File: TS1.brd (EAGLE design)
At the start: 32 x 22 mm, 20 parts, among them IC1 AT42QT1010, J1 PWR, Q1 2N7002

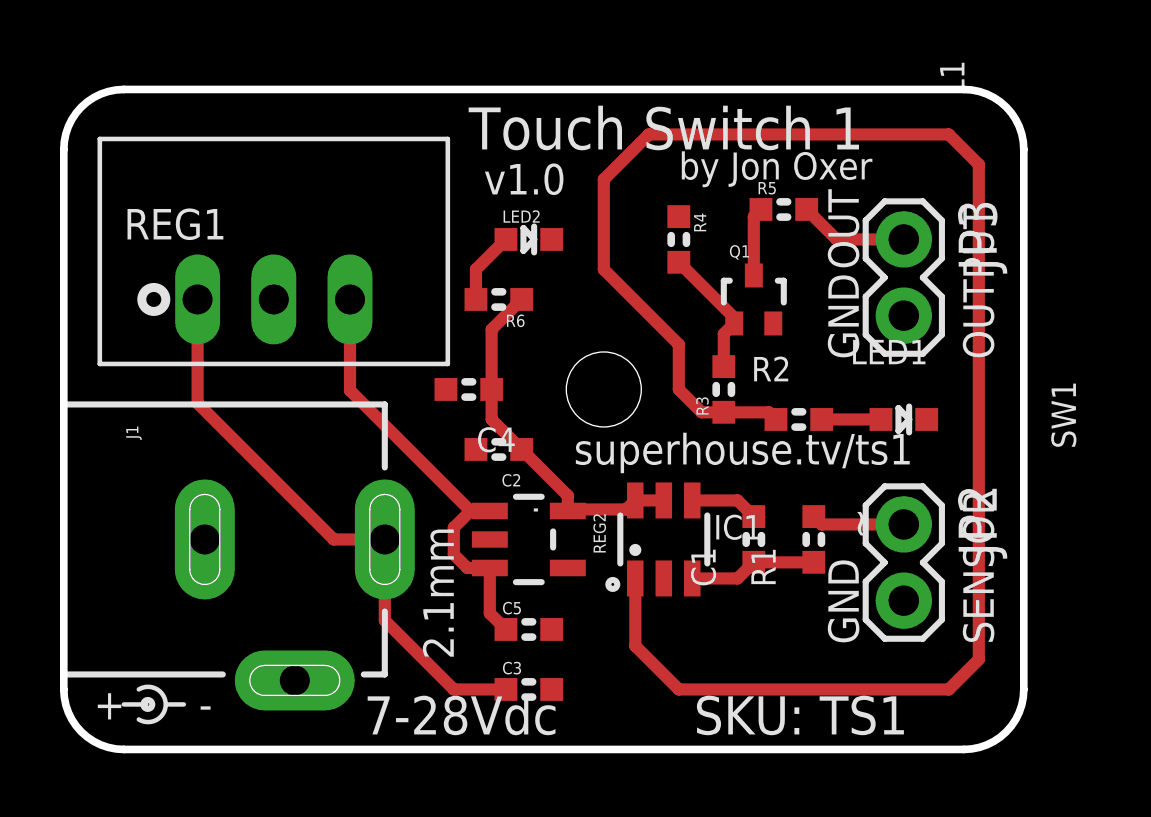
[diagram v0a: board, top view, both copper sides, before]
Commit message: Pulled back GND plane around input to sensor IC to reduce capacitive loading
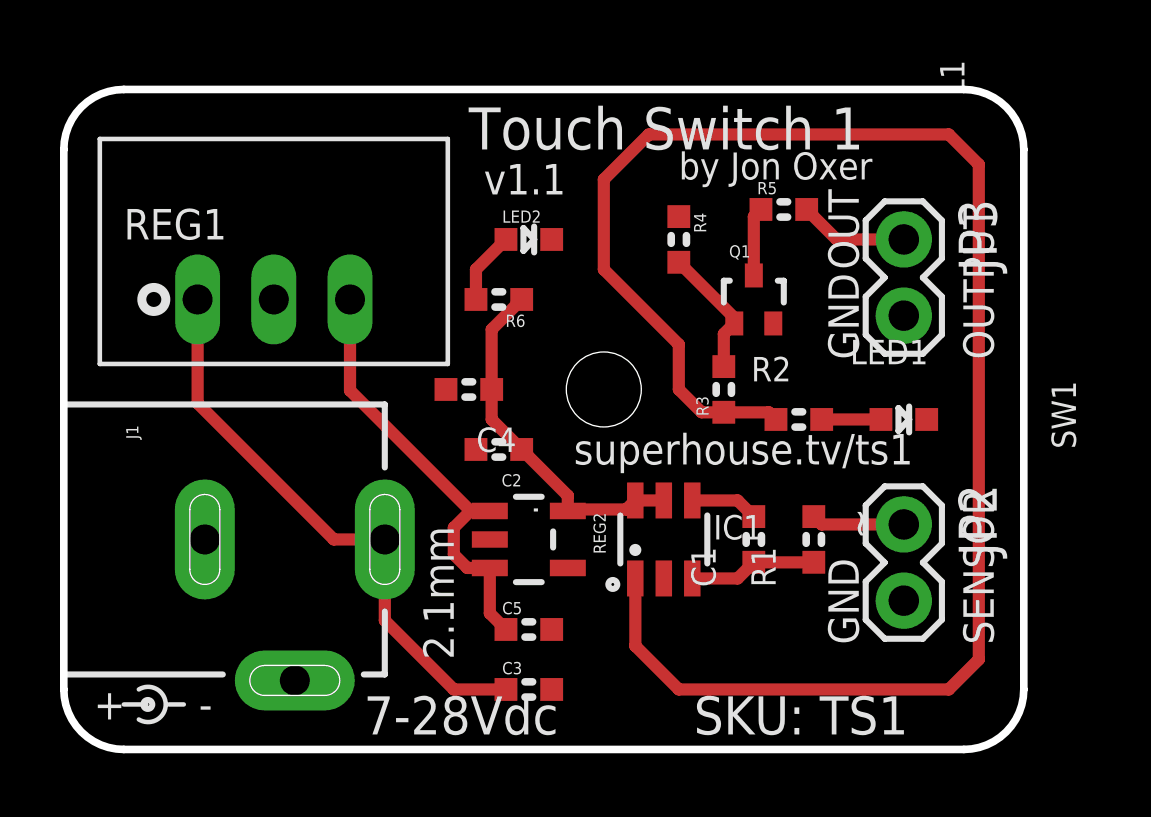
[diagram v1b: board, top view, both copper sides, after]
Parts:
- C2: value 10uF -> 100nF
- C4: value 100nF -> 10uF
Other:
- board text added: "Copyright 2019 SuperHouse Automation Pty Ltd"
- board text added: "v1.1"
- board text removed: "Copyright 2018 SuperHouse Automation Pty Ltd"
- board text removed: "v1.0"
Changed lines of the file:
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@@
 <?xml version="1.0" encoding="utf-8"?>
 <!DOCTYPE eagle SYSTEM "eagle.dtd">
-<eagle version="9.2.1">
+<eagle version="9.5.1">
 <drawing>
 <settings>
-<setting alwaysvectorfont="yes"/>
+<setting alwaysvectorfont="no"/>
 <setting keepoldvectorfont="yes"/>
 <setting verticaltext="up"/>
@@
 <layer number="14" name="Route14" color="1" fill="6" visible="no" active="no"/>
 <layer number="15" name="Route15" color="4" fill="6" visible="no" active="no"/>
-<layer number="16" name="Bottom" color="1" fill="1" visible="no" active="yes"/>
+<layer number="16" name="Bottom" color="1" fill="1" visible="yes" active="yes"/>
 <layer number="17" name="Pads" color="2" fill="1" visible="yes" active="yes"/>
 <layer number="18" name="Vias" color="2" fill="1" visible="yes" active="yes"/>
 <layer number="19" name="Unrouted" color="12" fill="1" visible="yes" active="yes"/>
 <layer number="20" name="Dimension" color="15" fill="1" visible="yes" active="yes"/>
-<layer number="21" name="tPlace" color="15" fill="1" visible="no" active="yes"/>
-<layer number="22" name="bPlace" color="14" fill="1" visible="no" active="yes"/>
+<layer number="21" name="tPlace" color="15" fill="1" visible="yes" active="yes"/>
+<layer number="22" name="bPlace" color="14" fill="1" visible="yes" active="yes"/>
 <layer number="23" name="tOrigins" color="15" fill="1" visible="yes" active="yes"/>
 <layer number="24" name="bOrigins" color="15" fill="1" visible="yes" active="yes"/>
@@
 <layer number="37" name="tTest" color="7" fill="1" visible="no" active="yes"/>
 <layer number="38" name="bTest" color="7" fill="1" visible="no" active="yes"/>
-<layer number="39" name="tKeepout" color="4" fill="11" visible="no" active="yes"/>
+<layer number="39" name="tKeepout" color="4" fill="11" visible="yes" active="yes"/>
 <layer number="40" name="bKeepout" color="1" fill="11" visible="no" active="yes"/>
-<layer number="41" name="tRestrict" color="4" fill="10" visible="no" active="yes"/>
-<layer number="42" name="bRestrict" color="1" fill="10" visible="no" active="yes"/>
+<layer number="41" name="tRestrict" color="4" fill="10" visible="yes" active="yes"/>
+<layer number="42" name="bRestrict" color="1" fill="10" visible="yes" active="yes"/>
 <layer number="43" name="vRestrict" color="2" fill="10" visible="no" active="yes"/>
 <layer number="44" name="Drills" color="7" fill="1" visible="no" active="yes"/>
@@
 <text x="26.5" y="13" size="1.016" layer="21" font="vector" ratio="16" rot="R90">GND</text>
 <text x="17" y="9.5" size="1.016" layer="21" font="vector" ratio="16">superhouse.tv/ts1</text>
-<text x="31" y="9.5" size="0.9" layer="22" font="vector" ratio="16" rot="MR0">Copyright 2018
+<text x="31" y="9.5" size="0.9" layer="22" font="vector" ratio="16" rot="MR0">Copyright 2019
 SuperHouse Automation Pty Ltd</text>
 <text x="26" y="2" size="1.016" layer="22" font="vector" ratio="16" rot="MR0">Released under
@@
 Hardware License
 tapr.org/OHL</text>
-<text x="14" y="18.5" size="1.016" layer="21" font="vector" ratio="16">v1.0</text>
+<text x="14" y="18.5" size="1.016" layer="21" font="vector" ratio="16">v1.1</text>
 <text x="13" y="3" size="1.016" layer="21" font="vector" ratio="16" rot="R90">2.1mm</text>
 <wire x1="2.5" y1="2" x2="2.5" y2="1" width="0.15" layer="21" curve="-243.434949"/>
@@
 <wire x1="2" y1="22" x2="0" y2="20" width="0.254" layer="20" curve="90"/>
 <wire x1="0" y1="20" x2="0" y2="2" width="0.254" layer="20"/>
+<wire x1="20.5" y1="9.5" x2="20.5" y2="4.5" width="0.0762" layer="41"/>
+<wire x1="20.5" y1="4.5" x2="25.25" y2="4.5" width="0.0762" layer="41"/>
+<wire x1="25.25" y1="4.5" x2="27" y2="6.25" width="0.0762" layer="41"/>
+<wire x1="27" y1="6.25" x2="30" y2="6.25" width="0.0762" layer="41"/>
+<wire x1="30" y1="6.25" x2="30" y2="9.5" width="0.0762" layer="41"/>
+<wire x1="30" y1="9.5" x2="20.5" y2="9.5" width="0.0762" layer="41"/>
+<wire x1="20.5" y1="9.5" x2="20.5" y2="4.5" width="0.0762" layer="42"/>
+<wire x1="20.5" y1="4.5" x2="25.25" y2="4.5" width="0.0762" layer="42"/>
+<wire x1="25.25" y1="4.5" x2="27" y2="6.25" width="0.0762" layer="42"/>
+<wire x1="27" y1="6.25" x2="30" y2="6.25" width="0.0762" layer="42"/>
+<wire x1="30" y1="6.25" x2="30" y2="9.5" width="0.0762" layer="42"/>
+<wire x1="30" y1="9.5" x2="20.5" y2="9.5" width="0.0762" layer="42"/>
 </plain>
 <attributes>
@@
 </autorouter>
 <elements>
-<element name="C2" library="freetronics-jon" library_urn="urn:adsk.eagle:library:7065448" package="0603" package3d_urn="urn:adsk.eagle:package:7066315/2" value="10uF" x="14.5" y="10" smashed="yes" rot="R180">
+<element name="C2" library="freetronics-jon" library_urn="urn:adsk.eagle:library:7065448" package="0603" package3d_urn="urn:adsk.eagle:package:7066315/2" value="100nF" x="14.5" y="10" smashed="yes" rot="R180">
 <attribute name="NAME" x="15.262" y="9.1745" size="0.4064" layer="25" rot="R180"/>
 <attribute name="VALUE" x="12.584" y="10.503" size="0.6096" layer="27"/>
@@
 <attribute name="VALUE" x="24.7126" y="8.349" size="0.6096" layer="27" ratio="10"/>
 </element>
-<element name="C4" library="freetronics-jon" library_urn="urn:adsk.eagle:library:7065448" package="0603" package3d_urn="urn:adsk.eagle:package:7066315/2" value="100nF" x="13.5" y="12" smashed="yes" rot="R180">
+<element name="C4" library="freetronics-jon" library_urn="urn:adsk.eagle:library:7065448" package="0603" package3d_urn="urn:adsk.eagle:package:7066315/2" value="10uF" x="13.5" y="12" smashed="yes" rot="R180">
 <attribute name="NAME" x="15.0875" y="10.73" size="0.8128" layer="25" ratio="18" rot="R180"/>
 <attribute name="VALUE" x="11.8126" y="12.549" size="0.6096" layer="27" ratio="10"/>

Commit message: Moved bypass cap closer to touch sensor IC
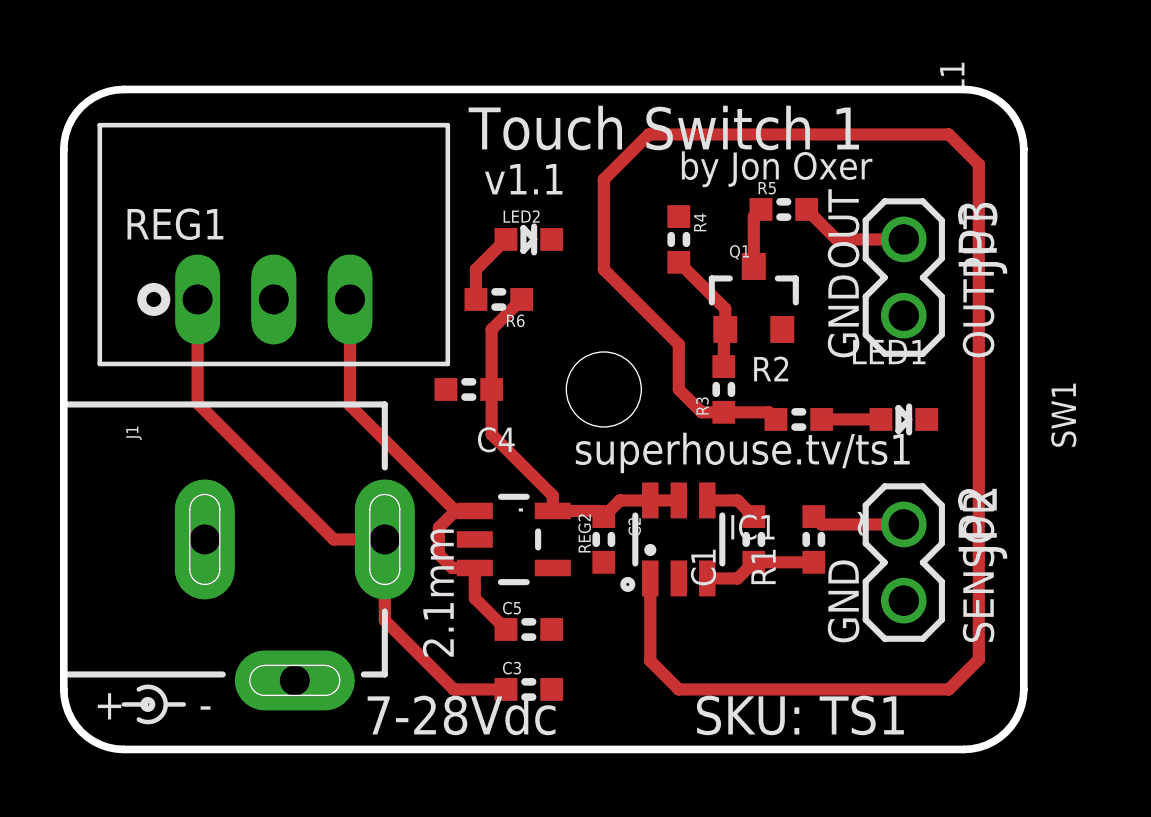
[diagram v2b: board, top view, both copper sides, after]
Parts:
- C1, C2, C3, C4, C5: device freetronics-jon:0603 -> SuperHouse-DiscreteSemi:C0603
- IC1: device microbuilder:SOT23-6 -> SuperHouse-ICs:SOT23-6
- J1: device freetronics-jon:POWER_JACK_PTH_SLOTS -> SuperHouse-Connectors:POWER_JACK_SLOTS
- JP2, JP3: device freetronics-jon:1X02 -> SuperHouse-Connectors:1X02-S
- LED1, LED2: device freetronics-jon:LED-0603 -> SuperHouse-LEDs:LED-0603
- Q1: device freetronics-jon:SOT32-3 -> SuperHouse-DiscreteSemi:SOT23-3
- R1, R2, R3, R4, R5, R6: device freetronics-jon:0603 -> SuperHouse-DiscreteSemi:R0603
- REG1: value K7803 -> K7805; device freetronics-jon:K78XX-500R3 -> SuperHouse-Regulators:K78XX-500R3
- REG2: device freetronics-jon:SOT23-5 -> SuperHouse-Regulators:SOT23-5
- moved C2 4.61 mm to (18.0, 7.00), turned to 270 degrees
- moved IC1 0.50 mm to (20.5, 7.00)
- moved REG2 0.50 mm to (15.0, 7.00)
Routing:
- net VDD: track 11.9 -> 12.9 mm
- net N$4: track 4.27 -> 3.77 mm
- net N$3: track 2.27 -> 1.77 mm
